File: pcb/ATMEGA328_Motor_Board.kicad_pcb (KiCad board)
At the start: 2 copper layers, 77 x 100 mm, 256 parts, among them P1 CONN_01X04, P10 CONN_01X04, P11 CONN_01X02, P12 CONN_01X03, P13 CONN_01X02, P14 USB_MINI, P15 CONN_01X03, P16 CONN_02X03, P2 CONN_01X04, P3 CONN_01X03, P4 CONN_01X03, P5 CONN_01X03, P6 CONN_01X03, P7 CONN_01X03, P8 CONN_01X03, P9 CONN_01X04, SW1 Pulsador_2p, U1 ATMEGA328, U10 VOM617A, U11 VOM617A, U12 ASSR-1218, U13 ASSR-1218, U2 PCA9685, U3 FT231X, U4 L298P, U5 L298P, U6 TSR_1, U7 LM2903, U8 LM2903, U9 VOM617A, Y1 16MHz

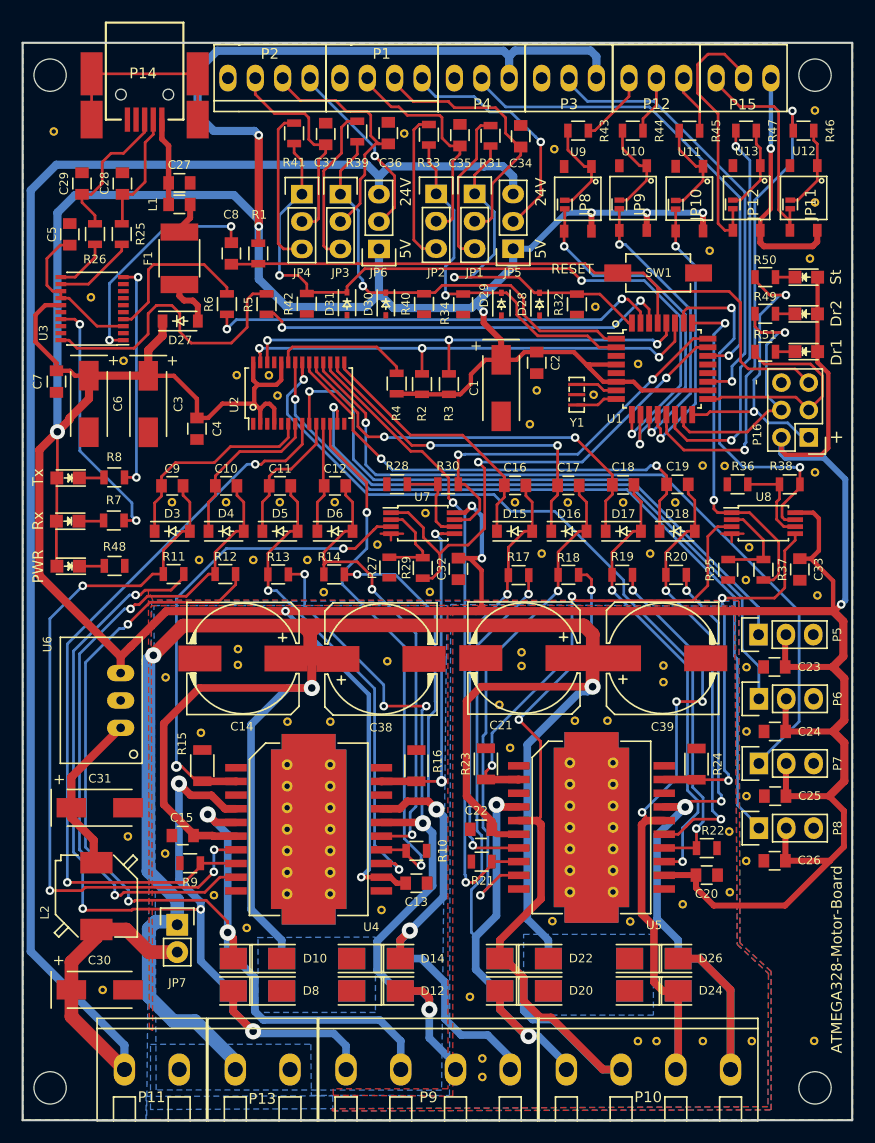
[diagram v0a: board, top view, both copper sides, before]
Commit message: correcciones menores y ecualizar longitud de pistas
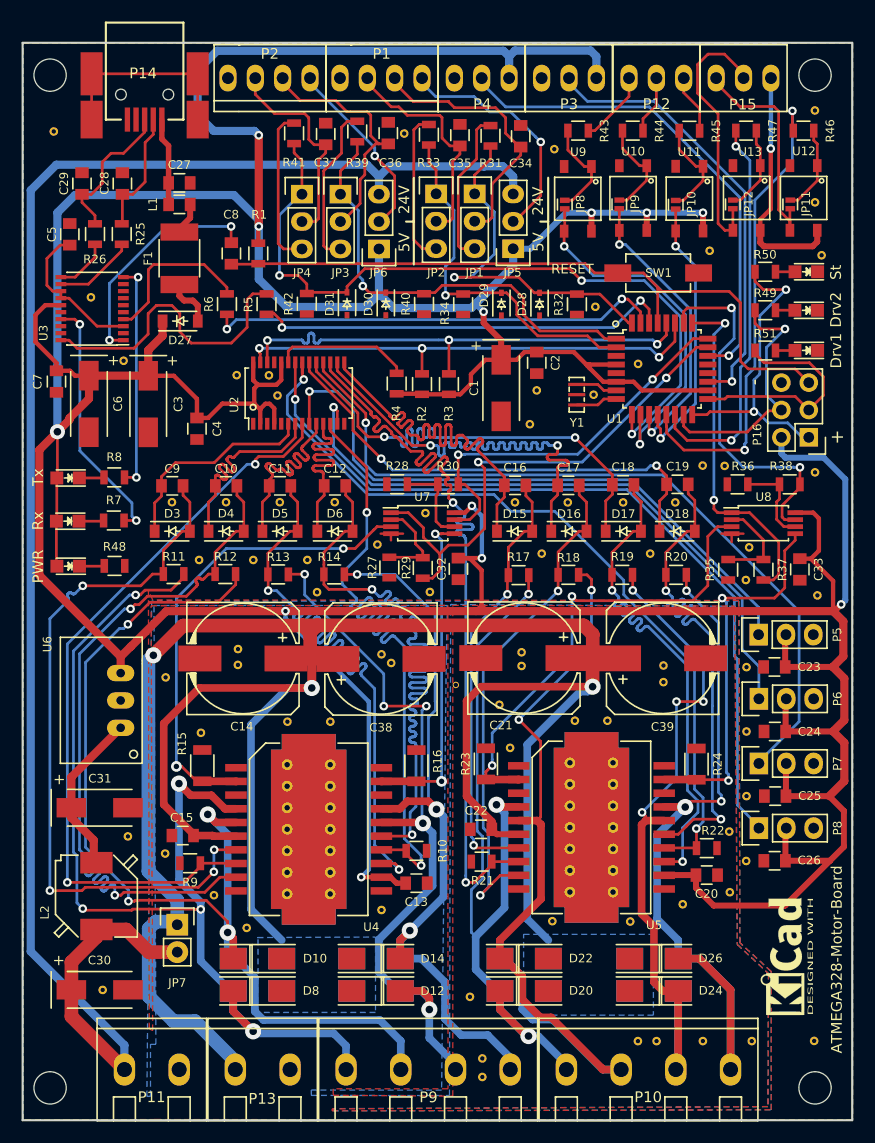
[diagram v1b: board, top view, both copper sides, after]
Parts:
- added G***: KiCad Logo, logos:KiCad-Logo_11mmx5mm, F.Cu at (179.0, 124.8)
- added Gnd-Via: VAL**, Vias:Gnd-Via, F.Cu at (142.7, 97.6)
- added Gnd-Via: VAL**, Vias:Gnd-Via, F.Cu at (148.7, 99.6)
- moved Gnd-Via 1.12 mm to (182.6, 59.7)
- moved Gnd-Via 0.84 mm to (141.8, 96.8)
- moved Gnd-Via 0.62 mm to (135.8, 91.0)
- moved D34 0.50 mm to (181.2, 61.2), turned to 180 degrees
- moved R50 0.50 mm to (177.4, 61.2)
- moved R49 0.33 mm to (177.4, 64.8)
- moved D33 0.33 mm to (181.2, 64.8), turned to 180 degrees
- moved D35 0.11 mm to (181.2, 68.5), turned to 180 degrees
- moved R51 0.11 mm to (177.4, 68.6)
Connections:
- D33 pad 1: Net-(D33-Pad1) -> GND
- D33 pad 2: +5V -> Net-(D33-Pad2)
- D34 pad 1: Net-(D34-Pad1) -> GND
- D34 pad 2: +5V -> Net-(D34-Pad2)
- D35 pad 1: Net-(D35-Pad1) -> GND
- D35 pad 2: +5V -> Net-(D35-Pad2)
- R49 pad 2: Net-(D33-Pad1) -> Net-(D33-Pad2)
- R50 pad 2: Net-(D34-Pad1) -> Net-(D34-Pad2)
- R51 pad 2: Net-(D35-Pad1) -> Net-(D35-Pad2)
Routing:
- net /Potencia/Motor2_B_in: track 44.4 -> 68.0 mm
- net /Potencia/Motor2_A_in: track 44.9 -> 68.0 mm
- net +5V: track 555.8 -> 533.5 mm
- net MOTOR2_EN: track 50.9 -> 69.0 mm
- net MOTOR3_A: track 24.9 -> 41.8 mm
- net MOTOR3_EN: track 60.0 -> 73.8 mm
- net MOTOR3_B: track 32.3 -> 45.5 mm
- net MOTOR2_B: track 10.3 -> 19.8 mm
- net /Potencia/Motor4_B_in: track 40.8 -> 48.2 mm
- net MOTOR4_A: track 38.5 -> 45.5 mm
- net MOTOR2_A: track 12.8 -> 19.7 mm
- net /Potencia/Motor1_B_in: track 61.3 -> 68.0 mm
- net /Potencia/Motor4_A_in: track 42.4 -> 48.1 mm
- net MOTOR1_B: track 15.6 -> 19.8 mm
- net VSS: track 228.3 -> 224.9 mm
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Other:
- rule pad_to_mask_clearance: 0.0762 -> 0.08
- board text added: "Drv1"
- board text added: "Drv2"
- board text removed: "Dr1"
- board text removed: "Dr2"

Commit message: modificar direccion I2C y pin /OE
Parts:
- moved Gnd-Via 5.23 mm to (127.9, 74.8)
- moved Gnd-Via 2.14 mm to (126.2, 70.8)
- moved Gnd-Via 1.01 mm to (131.3, 72.1)
- turned R4 to 270 degrees
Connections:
- R4 pad 1: +5V -> Net-(R4-Pad1)
- R4 pad 2: /Control/PWM_OE -> GND
- U2 pad 1: GND -> +5V
- U2 pad 2: +5V -> GND
- U2 pad 23: /Control/PWM_OE -> Net-(R4-Pad1)
- U2 pad 24: +5V -> GND
- U2 pad 3: GND -> +5V
- U2 pad 4: +5V -> GND
- U2 pad 5: GND -> +5V
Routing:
- net Net-(R4-Pad1): track 0.00 -> 12.6 mm
- net /Control/PWM_OE: track 12.6 -> 0.00 mm
- net +5V: track 533.5 -> 529.2 mm

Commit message: pcb lista para enviar a fabricar
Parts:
- moved G*** 0.27 mm to (179.2, 124.8)
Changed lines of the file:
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@@
     (mod_text_size 1 1)
     (mod_text_width 0.15)
-    (pad_size 0.6 0.6)
-    (pad_drill 0.4)
+    (pad_size 3 3)
+    (pad_drill 3)
     (pad_to_mask_clearance 0.08)
     (pad_to_paste_clearance -0.0762)
@@
     (add_net VSS)
   )
+  (module Conectores:usb_mini_molex_675031020 (layer F.Cu)
+    (at 119.775 47.125 270)
+    (fp_text reference P14 (at -4.295 0.145) (layer F.SilkS)
+      (effects (font (size 1 1) (thickness 0.15)))
+    )
+    (fp_text value USB_MINI (at -10.75 0) (layer F.Fab)
+      (effects (font (size 1 1) (thickness 0.15)))
+    )
+    (fp_line (start 0 3.6) (end 0 2.2) (layer F.SilkS) (width 0.2))
+    (fp_line (start 0 -3.6) (end 0 -2.2) (layer F.SilkS) (width 0.2))
+    (fp_line (start -9 3.6) (end 0 3.6) (layer F.SilkS) (width 0.2))
+    (fp_line (start -9 -3.6) (end -9 3.6) (layer F.SilkS) (width 0.2))
+    (fp_line (start 0 -3.6) (end -9 -3.6) (layer F.SilkS) (width 0.2))
+    (pad 3 smd rect (at 0 0 270) (size 2.25 0.5) (layers F.Cu F.Paste F.Mask)
+      (net 25 "Net-(C29-Pad1)"))
+    (pad 2 smd rect (at 0 -0.8 270) (size 2.25 0.5) (layers F.Cu F.Paste F.Mask)
+      (net 24 "Net-(C28-Pad1)"))
+    (pad 1 smd rect (at 0 -1.6 270) (size 2.25 0.5) (layers F.Cu F.Paste F.Mask)
+      (net 23 /Pines/XUSB))
+    (pad 4 smd rect (at 0 0.8 270) (size 2.25 0.5) (layers F.Cu F.Paste F.Mask)
+      (net 63 "Net-(P14-Pad4)"))
+    (pad 5 smd rect (at 0 1.6 270) (size 2.25 0.5) (layers F.Cu F.Paste F.Mask)
+      (net 1 GND))
+    (pad "" np_thru_hole circle (at -2.325 2.2 270) (size 1 1) (drill 1) (layers *.Cu F.SilkS))
+    (pad "" np_thru_hole circle (at -2.325 -2.2 270) (size 1 1) (drill 1) (layers *.Cu F.SilkS))
+    (pad 6 smd rect (at 0 -4.925 270) (size 3.5 2.05) (layers F.Cu F.Paste F.Mask)
+      (net 64 "Net-(P14-Pad6)"))
+    (pad 6 smd rect (at 0 4.925 270) (size 3.5 2.05) (layers F.Cu F.Paste F.Mask)
+      (net 64 "Net-(P14-Pad6)"))
+    (pad 6 smd rect (at -4.25 -4.925 270) (size 4 2.05) (layers F.Cu F.Paste F.Mask)
+      (net 64 "Net-(P14-Pad6)"))
+    (pad 6 smd rect (at -4.25 4.925 270) (size 4 2.05) (layers F.Cu F.Paste F.Mask)
+      (net 64 "Net-(P14-Pad6)"))
+    (model "../../../../../../Users/amorales/Documents/KiCad/usb mini/usb_mini_molex_675031020.wrl"
+      (at (xyz 0 0 0))
+      (scale (xyz 0.3937 0.3937 0.3937))
+      (rotate (xyz 0 0 0))
+    )
+    (model /home/amr/Documentos/KiCad/kicad-3d-modules/Conectores/usb_mini_molex_675031020.wrl
+      (at (xyz 0 0 0))
+      (scale (xyz 0.3937 0.3937 0.3937))
+      (rotate (xyz 0 0 0))
+    )
+  )
   (module Vias:Gnd-Via (layer F.Cu)
     (at 127.92 74.84)
@@
       (effects (font (size 1 1) (thickness 0.15)))
     )
-    (pad "" np_thru_hole circle (at 0 0) (size 3 3) (drill 3) (layers *.Cu *.Mask F.SilkS)
+    (pad "" np_thru_hole circle (at 0 0) (size 3 3) (drill 3) (layers *.Cu F.SilkS)
       (solder_mask_margin 1) (zone_connect 2))
   )
@@
       (effects (font (size 1 1) (thickness 0.15)))
     )
-    (pad "" np_thru_hole circle (at 0 0) (size 3 3) (drill 3) (layers *.Cu *.Mask F.SilkS)
+    (pad "" np_thru_hole circle (at 0 0) (size 3 3) (drill 3) (layers *.Cu F.SilkS)
       (solder_mask_margin 1) (zone_connect 2))
   )
@@
       (effects (font (size 1 1) (thickness 0.15)))
     )
-    (pad "" np_thru_hole circle (at 0 0) (size 3 3) (drill 3) (layers *.Cu *.Mask F.SilkS)
+    (pad "" np_thru_hole circle (at 0 0) (size 3 3) (drill 3) (layers *.Cu F.SilkS)
       (solder_mask_margin 1) (zone_connect 2))
   )
@@
       (effects (font (size 1 1) (thickness 0.15)))
     )
-    (pad "" np_thru_hole circle (at 0 0) (size 3 3) (drill 3) (layers *.Cu *.Mask F.SilkS)
+    (pad "" np_thru_hole circle (at 0 0) (size 3 3) (drill 3) (layers *.Cu F.SilkS)
       (solder_mask_margin 1) (zone_connect 2))
   )
@@
     )
   )
-  (module Conectores:usb_mini_molex_675031020 (layer F.Cu)
-    (at 119.775 47.125 270)
-    (fp_text reference P14 (at -4.295 0.145) (layer F.SilkS)
-      (effects (font (size 1 1) (thickness 0.15)))
-    )
-    (fp_text value USB_MINI (at -10.75 0) (layer F.Fab)
-      (effects (font (size 1 1) (thickness 0.15)))
-    )
-    (fp_line (start 0 3.6) (end 0 2.2) (layer F.SilkS) (width 0.2))
-    (fp_line (start 0 -3.6) (end 0 -2.2) (layer F.SilkS) (width 0.2))
-    (fp_line (start -9 3.6) (end 0 3.6) (layer F.SilkS) (width 0.2))
-    (fp_line (start -9 -3.6) (end -9 3.6) (layer F.SilkS) (width 0.2))
-    (fp_line (start 0 -3.6) (end -9 -3.6) (layer F.SilkS) (width 0.2))
-    (pad 3 smd rect (at 0 0 270) (size 2.25 0.5) (layers F.Cu F.Paste F.Mask)
-      (net 25 "Net-(C29-Pad1)"))
-    (pad 2 smd rect (at 0 -0.8 270) (size 2.25 0.5) (layers F.Cu F.Paste F.Mask)
-      (net 24 "Net-(C28-Pad1)"))
-    (pad 1 smd rect (at 0 -1.6 270) (size 2.25 0.5) (layers F.Cu F.Paste F.Mask)
-      (net 23 /Pines/XUSB))
-    (pad 4 smd rect (at 0 0.8 270) (size 2.25 0.5) (layers F.Cu F.Paste F.Mask)
-      (net 63 "Net-(P14-Pad4)"))
-    (pad 5 smd rect (at 0 1.6 270) (size 2.25 0.5) (layers F.Cu F.Paste F.Mask)
-      (net 1 GND))
-    (pad "" np_thru_hole circle (at -2.325 2.2 270) (size 1 1) (drill 1) (layers *.Cu *.Mask F.SilkS))
-    (pad "" np_thru_hole circle (at -2.325 -2.2 270) (size 1 1) (drill 1) (layers *.Cu *.Mask F.SilkS))
-    (pad 6 smd rect (at 0 -4.925 270) (size 3.5 2.05) (layers F.Cu F.Paste F.Mask)
-      (net 64 "Net-(P14-Pad6)"))
-    (pad 6 smd rect (at 0 4.925 270) (size 3.5 2.05) (layers F.Cu F.Paste F.Mask)
-      (net 64 "Net-(P14-Pad6)"))
-    (pad 6 smd rect (at -4.25 -4.925 270) (size 4 2.05) (layers F.Cu F.Paste F.Mask)
-      (net 64 "Net-(P14-Pad6)"))
-    (pad 6 smd rect (at -4.25 4.925 270) (size 4 2.05) (layers F.Cu F.Paste F.Mask)
-      (net 64 "Net-(P14-Pad6)"))
-    (model "../../../../../../Users/amorales/Documents/KiCad/usb mini/usb_mini_molex_675031020.wrl"
-      (at (xyz 0 0 0))
-      (scale (xyz 0.3937 0.3937 0.3937))
-      (rotate (xyz 0 0 0))
-    )
-    (model /home/amr/Documentos/KiCad/kicad-3d-modules/Conectores/usb_mini_molex_675031020.wrl
-      (at (xyz 0 0 0))
-      (scale (xyz 0.3937 0.3937 0.3937))
-      (rotate (xyz 0 0 0))
-    )
-  )
   (module Resistors_SMD:R_0805 (layer F.Cu)
     (at 130.325 59.55 270)
@@
   )
   (module logos:KiCad-Logo_11mmx5mm (layer F.Cu)
-    (at 178.98 124.8 90)
+    (at 179.25 124.77 90)
     (fp_text reference G*** (at -0.8 -1.6 90) (layer Cmts.User)
       (effects (font (size 0.3 0.3) (thickness 0.03)))
